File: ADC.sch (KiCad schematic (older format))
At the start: 4 parts

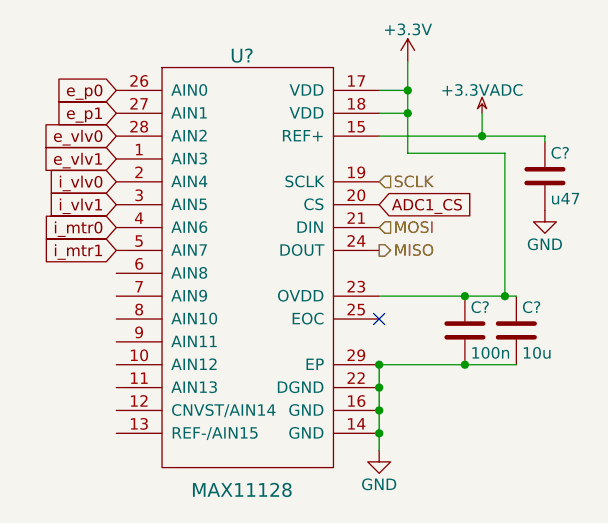
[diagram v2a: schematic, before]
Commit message: hotfix
fixed some labels
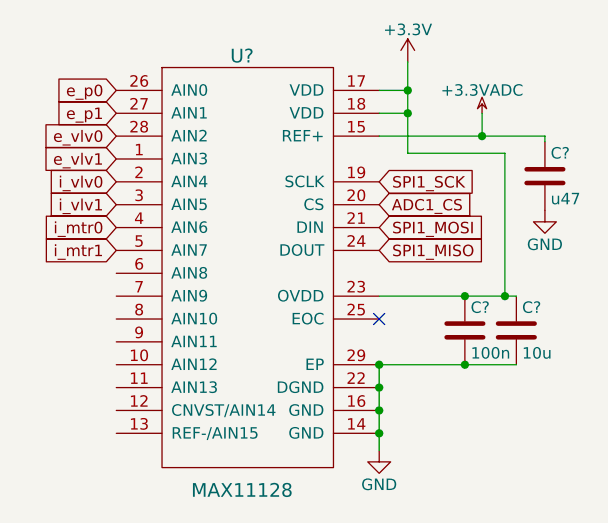
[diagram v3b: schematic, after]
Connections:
- net MISO renamed SPI1_MISO
- net MOSI renamed SPI1_MOSI
- net SCLK renamed SPI1_SCK
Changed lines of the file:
@@
 Wire Wire Line
 	6475 3300 6525 3300
-Text HLabel 5925 2800 2    50   Input ~ 0
-SCLK
-Text HLabel 5925 3000 2    50   Input ~ 0
-MOSI
-Text HLabel 5925 3100 2    50   Output ~ 0
-MISO
 Text GLabel 5925 2900 2    49   Input ~ 0
 ADC1_CS
@@
 Text GLabel 4775 3100 0    50   Input ~ 0
 i_mtr1
+Text GLabel 5925 3000 2    50   Input ~ 0
+SPI1_MOSI
+Text GLabel 5925 3100 2    50   Input ~ 0
+SPI1_MISO
+Text GLabel 5925 2800 2    50   Input ~ 0
+SPI1_SCK
 $EndSCHEMATC
